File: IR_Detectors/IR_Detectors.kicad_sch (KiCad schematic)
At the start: 22 parts, among them Q1 LTR-3208E, Q2 2N7000, U1 LM6144xIx, U2 MCP6294

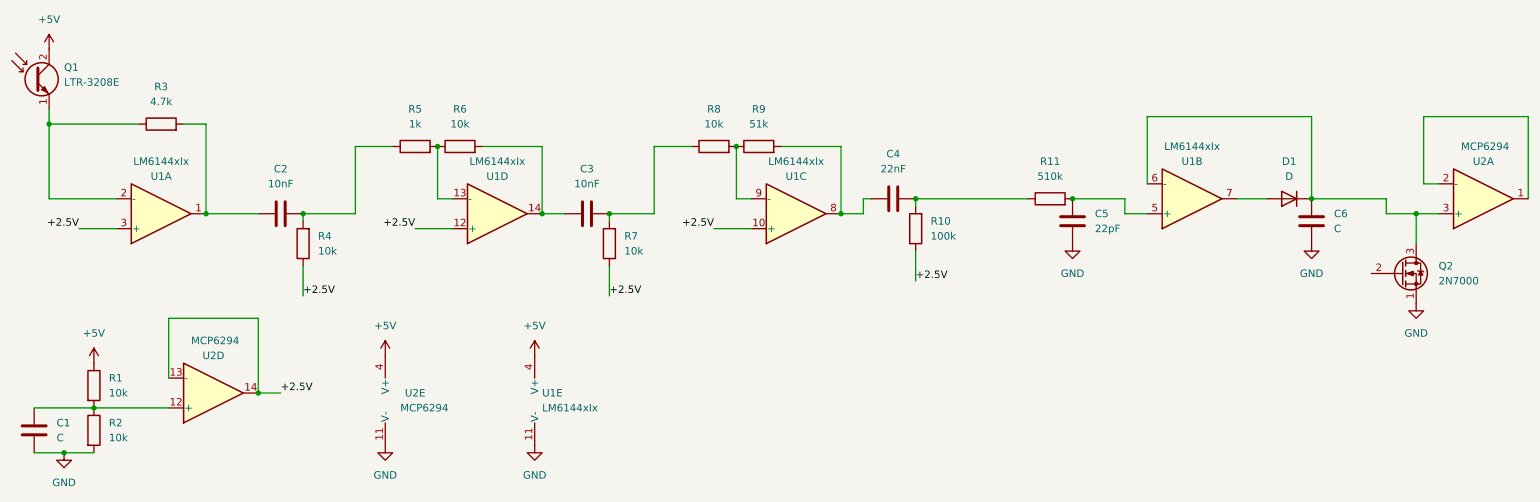
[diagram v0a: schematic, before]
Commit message: single IR detector design
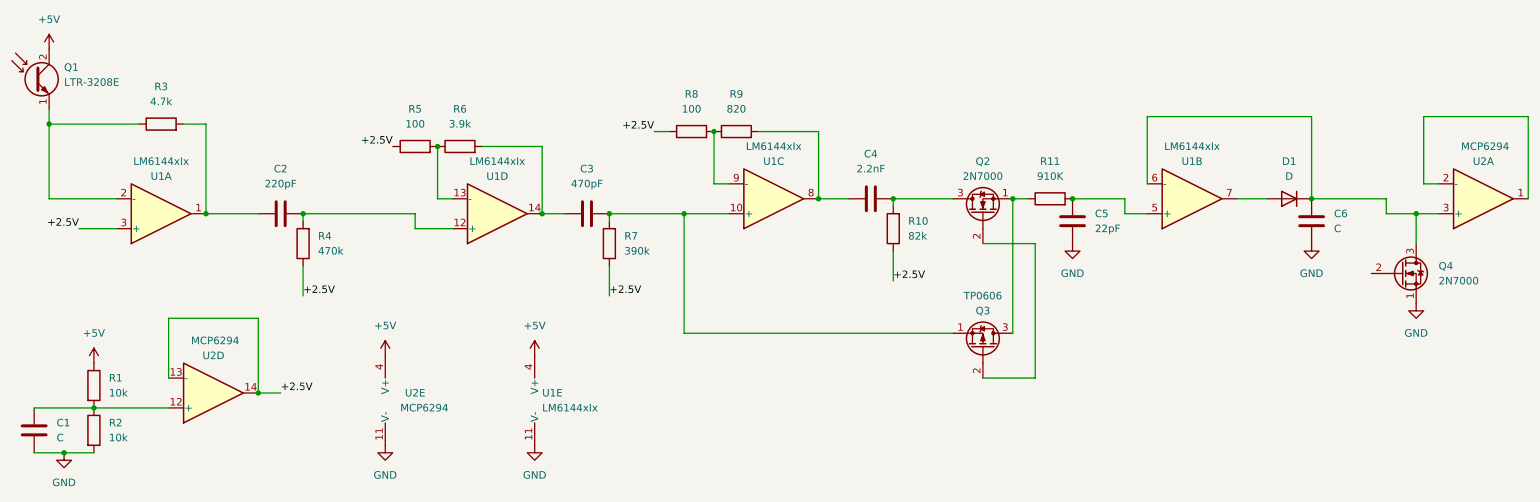
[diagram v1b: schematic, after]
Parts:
- added Q2: 2N7000, Package_TO_SOT_THT:TO-92_Inline, symbol Transistor_FET:2N7000
- added Q3: TP0606, Package_TO_SOT_THT:TO-92L_Inline, symbol Transistor_FET:TP0610L
- C2: value 10nF -> 220pF
- C3: value 10nF -> 470pF
- C4: value 22nF -> 2.2nF
- R10: value 100k -> 82k
- R11: value 510k -> 910K
- R4: value 10k -> 470k
- R5: value 1k -> 100
- R6: value 10k -> 3.9k
- R7: value 10k -> 390k
- R8: value 10k -> 100
- R9: value 51k -> 820
- renumbered Q2 to Q4
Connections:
- net +2.5V: now also R5.1, R8.1; no longer U1.10 (+), U1.12 (+)
- net at C4.2, R10.2: now also Q2.3 (D); no longer R11.1
- net at C2.2, R4.2: now also U1.12 (+); no longer R5.1
- net at C3.2, R7.2: now also U1.10 (+), Q3.1 (S); no longer R8.1
- new net: Q2.1 (S), Q3.3 (D), R11.1
- new net: Q2.2 (G), Q3.2 (G)

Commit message: updates
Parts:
- removed Q2: 2N7000, Package_TO_SOT_THT:TO-92_Inline, symbol Transistor_FET:2N7000
- removed Q3: TP0606, Package_TO_SOT_THT:TO-92L_Inline, symbol Transistor_FET:TP0610L
- added SW?: SW_DPDT_x2, symbol Switch:SW_DPDT_x2
- C3: value 470pF -> 4.7nF
- R5: value 100 -> 10
- R6: value 3.9k -> 390
- R7: value 390k -> 39k
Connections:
- net at C4.2, R10.2: now also SW?.4 (A)
- net at R11.1: now also SW?.5 (B)
- net at C3.2, R7.2, U1.10 (+): now also SW?.6 (C)
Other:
- note added: "may want to revert"
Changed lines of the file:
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@@
   (junction (at 29.21 102.87) (diameter 0) (color 0 0 0 0)
   )
+  (junction (at 110.49 62.23) (diameter 0) (color 0 0 0 0)
+  )
   (junction (at 170.18 59.69) (diameter 0) (color 0 0 0 0)
   )
-  (junction (at 110.49 62.23) (diameter 0) (color 0 0 0 0)
-  )
   (junction (at 69.85 62.23) (diameter 0) (color 0 0 0 0)
   )
@@
   (junction (at 53.34 62.23) (diameter 0) (color 0 0 0 0)
   )
-  (junction (at 190.5 59.69) (diameter 0) (color 0 0 0 0)
-  )
   (wire (pts (xy 69.85 71.12) (xy 69.85 76.2))
     (stroke (width 0) (type default))
@@
     (stroke (width 0) (type default))
   )
-  (wire (pts (xy 170.18 59.69) (xy 180.34 59.69))
-    (stroke (width 0) (type default))
-  )
   (wire (pts (xy 170.18 68.58) (xy 170.18 73.66))
     (stroke (width 0) (type default))
@@
     (stroke (width 0) (type default))
   )
-  (wire (pts (xy 185.42 67.31) (xy 194.31 67.31))
-    (stroke (width 0) (type default))
-  )
   (wire (pts (xy 260.35 57.15) (xy 260.35 45.72))
     (stroke (width 0) (type default))
@@
     (stroke (width 0) (type default))
   )
+  (wire (pts (xy 180.34 57.15) (xy 170.18 57.15))
+    (stroke (width 0) (type default))
+  )
   (wire (pts (xy 24.13 95.25) (xy 34.29 95.25))
     (stroke (width 0) (type default))
@@
     (stroke (width 0) (type default))
   )
+  (wire (pts (xy 170.18 57.15) (xy 170.18 59.69))
+    (stroke (width 0) (type default))
+  )
   (wire (pts (xy 260.35 45.72) (xy 278.13 45.72))
     (stroke (width 0) (type default))
@@
     (stroke (width 0) (type default))
   )
-  (wire (pts (xy 190.5 82.55) (xy 190.5 59.69))
-    (stroke (width 0) (type default))
-  )
   (wire (pts (xy 121.92 71.12) (xy 121.92 76.2))
     (stroke (width 0) (type default))
@@
     (stroke (width 0) (type default))
   )
-  (wire (pts (xy 194.31 90.17) (xy 185.42 90.17))
-    (stroke (width 0) (type default))
-  )
   (wire (pts (xy 254 62.23) (xy 259.08 62.23))
     (stroke (width 0) (type default))
@@
     (stroke (width 0) (type default))
   )
-  (wire (pts (xy 194.31 67.31) (xy 194.31 90.17))
-    (stroke (width 0) (type default))
-  )
   (wire (pts (xy 46.99 95.25) (xy 34.29 95.25))
     (stroke (width 0) (type default))
@@
     (stroke (width 0) (type default))
   )
+  (wire (pts (xy 180.34 62.23) (xy 180.34 82.55))
+    (stroke (width 0) (type default))
+  )
   (wire (pts (xy 134.62 82.55) (xy 180.34 82.55))
     (stroke (width 0) (type default))
@@
   (wire (pts (xy 46.99 80.01) (xy 62.23 80.01))
     (stroke (width 0) (type default))
+  )
+  (text "may want to revert\n" (at 90.17 40.64 0)
+    (effects (font (size 1.27 1.27)) (justify left bottom))
   )
   (label "+2.5V" (at 66.04 92.71 0) (fields_autoplaced)
@@
         (path "/abfb4fce-655e-4381-8d88-94d9bb99708e"
           (reference "#PWR04") (unit 1)
+        )
+      )
+    )
+  )
+  (symbol (lib_id "Switch:SW_DPDT_x2") (at 185.42 59.69 0) (mirror y) (unit 2)
+    (in_bom yes) (on_board yes) (dnp no)
+    (property "Reference" "SW?" (at 185.42 50.8 0)
+      (effects (font (size 1.27 1.27)))
+    )
+    (property "Value" "SW_DPDT_x2" (at 185.42 53.34 0)
+      (effects (font (size 1.27 1.27)))
+    )
+    (property "Footprint" "" (at 185.42 59.69 0)
+      (effects (font (size 1.27 1.27)) hide)
+    )
+    (property "Datasheet" "~" (at 185.42 59.69 0)
+      (effects (font (size 1.27 1.27)) hide)
+    )
+    (pin "1")
+    (pin "6")
+    (pin "5")
+    (pin "4")
+    (pin "3")
+    (pin "2")
+    (instances
+      (project "IR_Detectors"
+        (path "/abfb4fce-655e-4381-8d88-94d9bb99708e"
+          (reference "SW?") (unit 2)
         )
       )
@@
       (effects (font (size 1.27 1.27)))
     )
-    (property "Value" "100" (at 88.9 46.99 90)
+    (property "Value" "10" (at 88.9 46.99 90)
       (effects (font (size 1.27 1.27)))
     )
@@
       (effects (font (size 1.27 1.27)) (justify right))
     )
-    (property "Value" "390k" (at 124.46 68.58 0)
+    (property "Value" "39k" (at 124.46 68.58 0)
       (effects (font (size 1.27 1.27)) (justify right))
     )
@@
       (effects (font (size 1.27 1.27)))
     )
-    (property "Value" "3.9k" (at 96.52 46.99 90)
+    (property "Value" "390" (at 96.52 46.99 90)
       (effects (font (size 1.27 1.27)))
     )
@@
         (path "/abfb4fce-655e-4381-8d88-94d9bb99708e"
           (reference "R6") (unit 1)
-        )
-      )
-    )
-  )
-  (symbol (lib_id "Transistor_FET:TP0610L") (at 185.42 85.09 270) (mirror x) (unit 1)
-    (in_bom yes) (on_board yes) (dnp no)
-    (property "Reference" "Q3" (at 185.42 78.74 90)
-      (effects (font (size 1.27 1.27)))
-    )
-    (property "Value" "TP0606" (at 185.42 76.2 90)
-      (effects (font (size 1.27 1.27)))
-    )
-    (property "Footprint" "Package_TO_SOT_THT:TO-92L_Inline" (at 183.515 80.01 0)
-      (effects (font (size 1.27 1.27) italic) (justify left) hide)
-    )
-    (property "Datasheet" "http://www.vishay.com/docs/70209/70209.pdf" (at 181.61 80.01 0)
-      (effects (font (size 1.27 1.27)) (justify left) hide)
-    )
-    (pin "1")
-    (pin "3")
-    (pin "2")
-    (instances
-      (project "IR_Detectors"
-        (path "/abfb4fce-655e-4381-8d88-94d9bb99708e"
-          (reference "Q3") (unit 1)
         )
       )
@@
       (effects (font (size 1.27 1.27)))
     )
-    (property "Value" "470pF" (at 118.11 57.15 90)
+    (property "Value" "4.7nF" (at 118.11 57.15 90)
       (effects (font (size 1.27 1.27)))
     )
@@
         )
       )
-    )
-  )
-  (symbol (lib_id "Transistor_FET:2N7000") (at 185.42 62.23 90) (unit 1)
-    (in_bom yes) (on_board yes) (dnp no) (fields_autoplaced)
-    (property "Reference" "Q2" (at 185.42 53.34 90)
-      (effects (font (size 1.27 1.27)))
-    )
-    (property "Value" "2N7000" (at 185.42 55.88 90)
-      (effects (font (size 1.27 1.27)))
-    )
-    (property "Footprint" "Package_TO_SOT_THT:TO-92_Inline" (at 187.325 57.15 0)
-      (effects (font (size 1.27 1.27) italic) (justify left) hide)
-    )
-    (property "Datasheet" "https://www.vishay.com/docs/70226/70226.pdf" (at 189.23 57.15 0)
-      (effects (font (size 1.27 1.27)) (justify left) hide)
-    )
-    (pin "2")
-    (pin "1")
-    (pin "3")
-    (instances
-      (project "IR_Detectors"
-        (path "/abfb4fce-655e-4381-8d88-94d9bb99708e"
-          (reference "Q2") (unit 1)
-        )
-      )

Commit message: ir detector schematic
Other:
- note removed: "may want to revert"
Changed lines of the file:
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@@
     (stroke (width 0) (type default))
-  )
-  (text "may want to revert\n" (at 90.17 40.64 0)
-    (effects (font (size 1.27 1.27)) (justify left bottom))
   )
   (label "+2.5V" (at 66.04 92.71 0) (fields_autoplaced)
